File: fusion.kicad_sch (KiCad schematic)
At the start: 49 parts, among them J1 Conn_01x04_Female, J2 USB_C_Receptacle_USB2.0, J3 Conn_01x12_MountingPin, J4 Conn_01x12_MountingPin, K19 diode-choc, K20 diode-choc, K21 diode-choc, K22 diode-choc, K23 diode-choc, K24 diode-choc, K25 diode-choc, K26 diode-choc, K27 diode-choc, K28 diode-choc, K29 diode-choc, K30 diode-choc, K31 diode-choc, K32 diode-choc, K33 diode-choc, K34 diode-choc, K35 diode-choc, K36 diode-choc, K37 diode-choc, K38 diode-choc, SW1 SW_Push, U1 Holyiot_18010, U2 MT25QL128ABA1ESE

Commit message: final?
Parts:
- removed D42: SK6812MINI, LED_SMD:LED_SK6812MINI_PLCC4_3.5x3.5mm_P1.75mm, symbol LED:SK6812MINI
- removed U1: Holyiot_18010, keeb-libs:Holyiot-18010, symbol keeb-libs:Holyiot_18010
- added D2: LED_RBAG, fusion:FM-B2020RGBA, symbol Device:LED_RBAG
- added H15: sensor-magnet, fusion:sensor-magnet, symbol Mechanical:MountingHole
- added H16, H17, H18, H19: mount-magnet, fusion:mount-magnet, symbol Mechanical:MountingHole
- added R12: 1.2k, Resistor_SMD:R_0603_1608Metric, symbol Device:R
- added R13: 1.5k, Resistor_SMD:R_0603_1608Metric, symbol Device:R
- added R14: 1k, Resistor_SMD:R_0603_1608Metric, symbol Device:R
- added U1: Holyiot_18010_no_underside, keeb-libs:Holyiot-18010-no-underside, symbol keeb-libs:Holyiot_18010_no_underside
- H10, H7, H8, H9: value hinge -> mount-magnet; footprint fusion:hinge -> fusion:mount-magnet
- J1: footprint keeb-libs:debug-port -> keeb-libs:debug-port-single-side
- R3: value 10k -> 100k
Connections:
- net BAT_MEAS: now also U1.11 ([L]_A7_P0.31)
- net C0: now also U1.39 ([L]_P1.02)
- net C1: now also U1.36 ([L]_P1.04)
- net C2: now also U1.35 ([L]_P1.06)
- net C3: now also U1.34 ([L]_P0.09)
- net C4: now also U1.33 ([L]_P0.10)
- net D+: now also U1.45 (D+)
- net D-: now also U1.46 (D-)
- net DISP_~{CS}: now also U1.6 ([L]_A1_P0.03)
- net FLASH_~{CS}: now also U1.8 ([L]_A4_P0.28)
- net GND: now also U1.1 (GND), U1.32 (GND), U1.44 (GND)
- net MISO_DQ1: now also U1.12 (A2_P0.04)
- net MOSI_DQ0: now also U1.13 (A3_P0.05)
- net MOTION: now also U1.7 ([L]_A0_P0.02)
- net R0: now also U1.5 ([L]_P1.15)
- net R1: now also U1.4 ([L]_P1.13)
- net R2: now also U1.3 ([L]_P1.10)
- net R3: now also U1.2 ([L]_P1.11)
- net R4: now also U1.41 ([L]_P1.03)
- net R5: now also U1.43 (P0.22)
- net R6: now also U1.52 (P0.12)
- net R7: now also U1.53 (P1.09)
- net RST: now also U1.48 (Reset/P0.18)
- net SCLK: now also U1.54 (P0.07)
- net SHTDWN: now also U1.9 ([L]_A5_P0.29)
- net SWC: now also J1.3 (Pin_3), U1.38 (SWC); no longer J1.4 (Pin_4)
- net SWD: now also J1.4 (Pin_4), U1.37 (SWD); no longer J1.3 (Pin_3)
- net TRACKPAD_~{CS}: now also U1.10 ([L]_A6_P0.30)
- net VBUS: now also U1.47 (VBUS)
- net VDD: now also D2.3 (A), U1.55 (VDD)
- new net: D2.4 (GK), R13.2
- new net: D2.1 (RK), R12.2
- new net: D2.2 (BK), R14.2
- new net MAGNET: U1.40 ([L]_P1.01)
- new net ~{BLUE}: R14.1, U1.49 (P0.19)
- new net ~{GREEN}: R13.1, U1.50 (P0.21)
- new net ~{RED}: R12.1, U1.51 (P0.23)
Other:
- removed sheet trackpad_conn
- added sheet trackpad-8520 (trackpad-8520.kicad_sch)
- sheet power ports: added MAGNET; removed GND
- moved on the sheet: H11, H12, H13, H14, H3, H4

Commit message: backup
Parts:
- removed D2: LED_RBAG, fusion:FM-B2020RGBA, symbol Device:LED_RBAG
- removed H10, H16, H19: mount-magnet, fusion:mount-magnet, symbol Mechanical:MountingHole
- added D2: LED_RABG, LED_SMD:LED_ASMB-KTF0-0A306, symbol Device:LED_RABG
- added H20: bat-cover, fusion:bat-cover, symbol Mechanical:MountingHole
- added H21, H22, H23, H24: hinge-mousebite, fusion:hinge-mousebite, symbol Mechanical:MountingHole
- added JP1, JP2, JP3: SolderJumper_2_Open, Jumper:SolderJumper-2_P1.3mm_Open_RoundedPad1.0x1.5mm, symbol Jumper:SolderJumper_2_Open
- added U8: SRV05-4, Package_TO_SOT_SMD:SOT-23-6, symbol Power_Protection:SRV05-4
- H7: value mount-magnet -> hinge; footprint fusion:mount-magnet -> fusion:hinge
- K19, K24, K29: footprint pg1232:pg1232-DSSL -> pg1232:pg1232-DSSN
- K20, K25, K30: footprint pg1232:pg1232-DSSR -> pg1232:pg1232-DSSL
- K22, K27, K32: footprint pg1232:pg1232-DSSL -> pg1232:pg1232-DSSR
- K23, K28, K33: footprint pg1232:pg1232-DSSN -> pg1232:pg1232-DSSL
- K34, K35: footprint pg1232:pg1232-DSS -> pg1232:pg1232-DSSN
- K37, K38: footprint pg1232:pg1232-DSSN -> pg1232:pg1232-DSS
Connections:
- net C0: now also J4.4 (Pin_4), U1.2 ([L]_P1.11); no longer J4.12 (Pin_12), U1.39 ([L]_P1.02)
- net C1: now also J4.5 (Pin_5), U1.3 ([L]_P1.10); no longer J4.11 (Pin_11), U1.36 ([L]_P1.04)
- net C2: now also J4.6 (Pin_6), U1.4 ([L]_P1.13); no longer J4.10 (Pin_10), U1.35 ([L]_P1.06)
- net C3: now also J4.7 (Pin_7), U1.5 ([L]_P1.15); no longer J4.9 (Pin_9), U1.34 ([L]_P0.09)
- net D+: now also U8.3 (IO2), U8.4 (IO3)
- net D-: now also U8.1 (IO1), U8.6 (IO4)
- net FLASH_~{CS}: now also U1.53 (P1.09); no longer U1.8 ([L]_A4_P0.28)
- net GND: now also U8.2 (VN)
- net MISO_DQ1: now also JP2.2 (B)
- net MOSI_DQ0: now also JP3.2 (B)
- net R0: now also J4.9 (Pin_9), U1.34 ([L]_P0.09); no longer J4.7 (Pin_7), U1.5 ([L]_P1.15)
- net R1: now also J4.10 (Pin_10), U1.35 ([L]_P1.06); no longer J4.6 (Pin_6), U1.4 ([L]_P1.13)
- net R2: now also J4.11 (Pin_11), U1.36 ([L]_P1.04); no longer J4.5 (Pin_5), U1.3 ([L]_P1.10)
- net R3: now also J4.12 (Pin_12), U1.39 ([L]_P1.02); no longer J4.4 (Pin_4), U1.2 ([L]_P1.11)
- net R7: now also U1.8 ([L]_A4_P0.28); no longer U1.53 (P1.09)
- net SCLK: now also JP1.2 (B)
- net VBUS: now also U8.5 (VP)
- net VDD: now also D2.2 (A)
- net left/BAT: now also J3.12 (Pin_12); no longer J3.1 (Pin_1)
- net left/C0: now also J3.9 (Pin_9); no longer J3.12 (Pin_12)
- net left/C1: now also J3.8 (Pin_8); no longer J3.11 (Pin_11)
- net left/C2: now also J3.7 (Pin_7); no longer J3.10 (Pin_10)
- net left/C3: now also J3.6 (Pin_6); no longer J3.9 (Pin_9)
- net left/C4: now also J3.5 (Pin_5); no longer J3.8 (Pin_8)
- net left/GND: now also J3.11 (Pin_11); no longer J3.2 (Pin_2)
- net left/R0: now also J3.4 (Pin_4); no longer J3.7 (Pin_7)
- net left/R1: now also J3.3 (Pin_3); no longer J3.6 (Pin_6)
- net left/R2: now also J3.2 (Pin_2); no longer J3.5 (Pin_5)
- net left/R3: now also J3.1 (Pin_1); no longer J3.4 (Pin_4)
- net at R13.2: now also D2.4 (GK)
- net at R12.2: now also D2.1 (RK)
- net at R14.2: now also D2.3 (BK)
- new net trackpad-8520/MISO_2V8: JP2.1 (A)
- new net trackpad-8520/MOSI_3V3: JP3.1 (A)
- new net trackpad-8520/SCK_3V3: JP1.1 (A)
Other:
- moved on the sheet: H11, H13, H3, H4, H5, H6, J2, J3, R7, R9

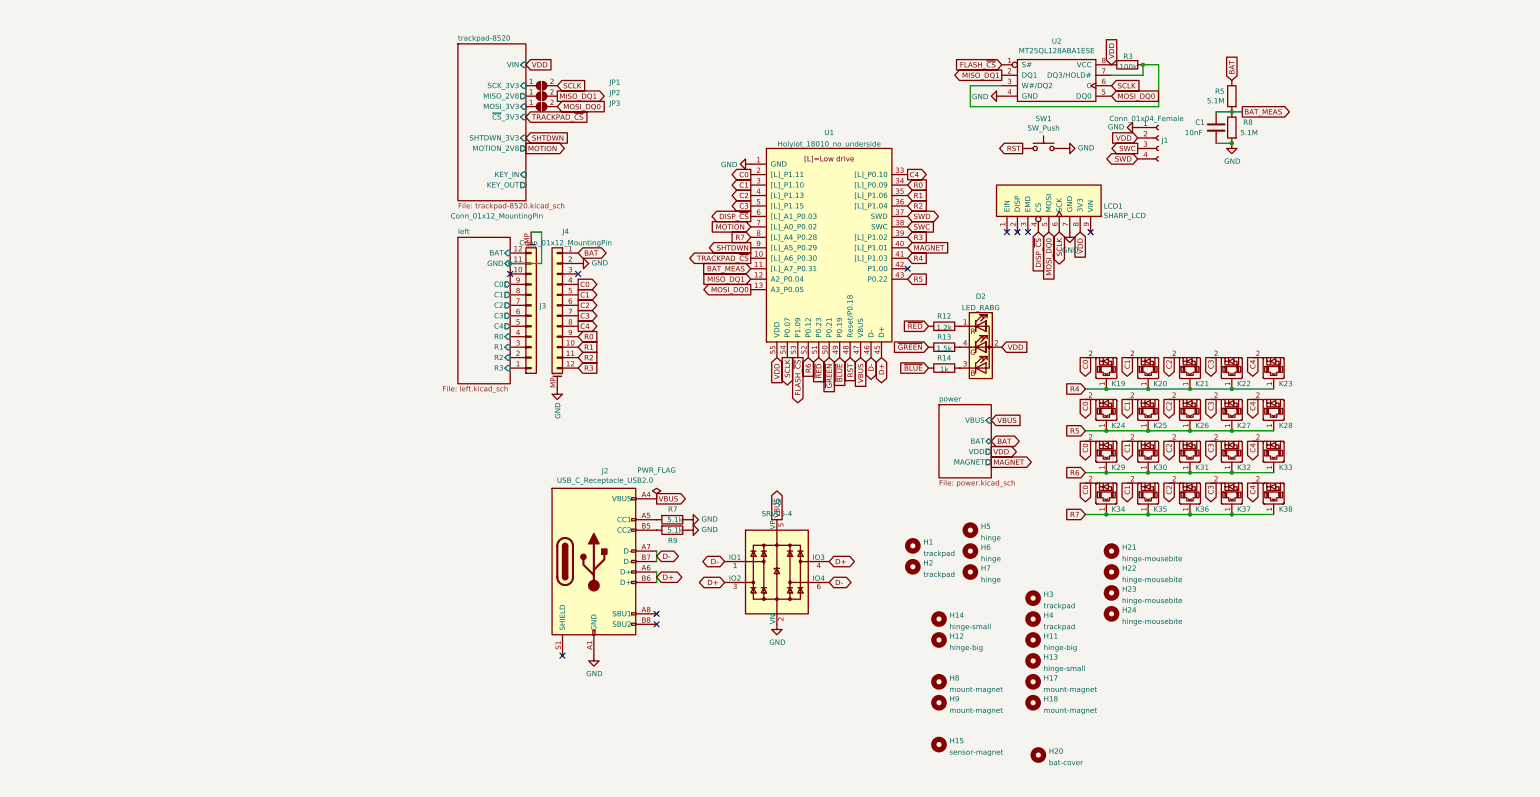
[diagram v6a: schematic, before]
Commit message: Hydrogen.PCB
- add Adafruit CAD files for Sharp display
- convert to all 3D printed mechanical parts
- update part dimensions to lowest estimate
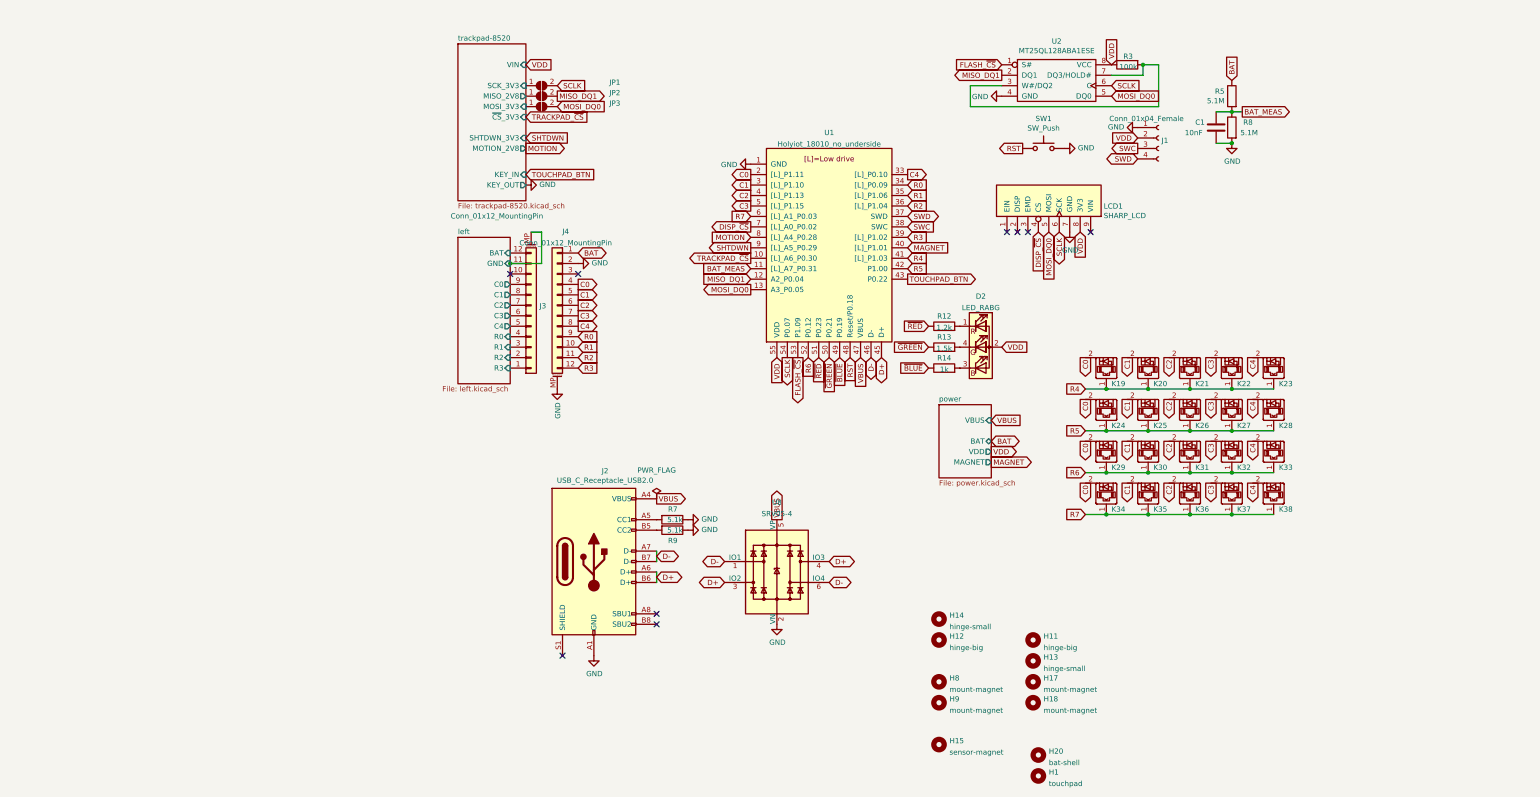
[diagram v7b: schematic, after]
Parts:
- removed H2, H3, H4: trackpad, fusion:trackpad, symbol Mechanical:MountingHole
- removed H21, H22, H23, H24: hinge-mousebite, fusion:hinge-mousebite, symbol Mechanical:MountingHole
- removed H5, H6, H7: hinge, fusion:hinge, symbol Mechanical:MountingHole
- D2, H15, H17, H18, H8, H9, J1, J3, J4, LCD1, U1: now left out of the parts list
- H1: value trackpad -> touchpad; footprint fusion:trackpad -> fusion:touchpad-holder; now left out of the parts list
- H11, H12: footprint fusion:hinge-big -> fusion:hinge2; now left out of the parts list
- H13, H14: footprint fusion:hinge-small -> fusion:hinge1; now left out of the parts list
- H20: value bat-cover -> bat-shell; footprint fusion:bat-cover -> fusion:bat-shell; now left out of the parts list
- SW1: footprint Button_Switch_SMD:SW_SPST_B3U-1000P -> Button_Switch_SMD:SW_SPST_TL3342
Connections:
- net DISP_~{CS}: now also U1.7 ([L]_A0_P0.02); no longer U1.6 ([L]_A1_P0.03)
- net MOTION: now also U1.8 ([L]_A4_P0.28); no longer U1.7 ([L]_A0_P0.02)
- net R5: now also U1.42 (P1.00); no longer U1.43 (P0.22)
- net R7: now also U1.6 ([L]_A1_P0.03); no longer U1.8 ([L]_A4_P0.28)
- new net TOUCHPAD_BTN: U1.43 (P0.22)
- no-connect marks 10 -> 9

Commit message: update PCB
use cirque trackpad, increase angle to 22.5
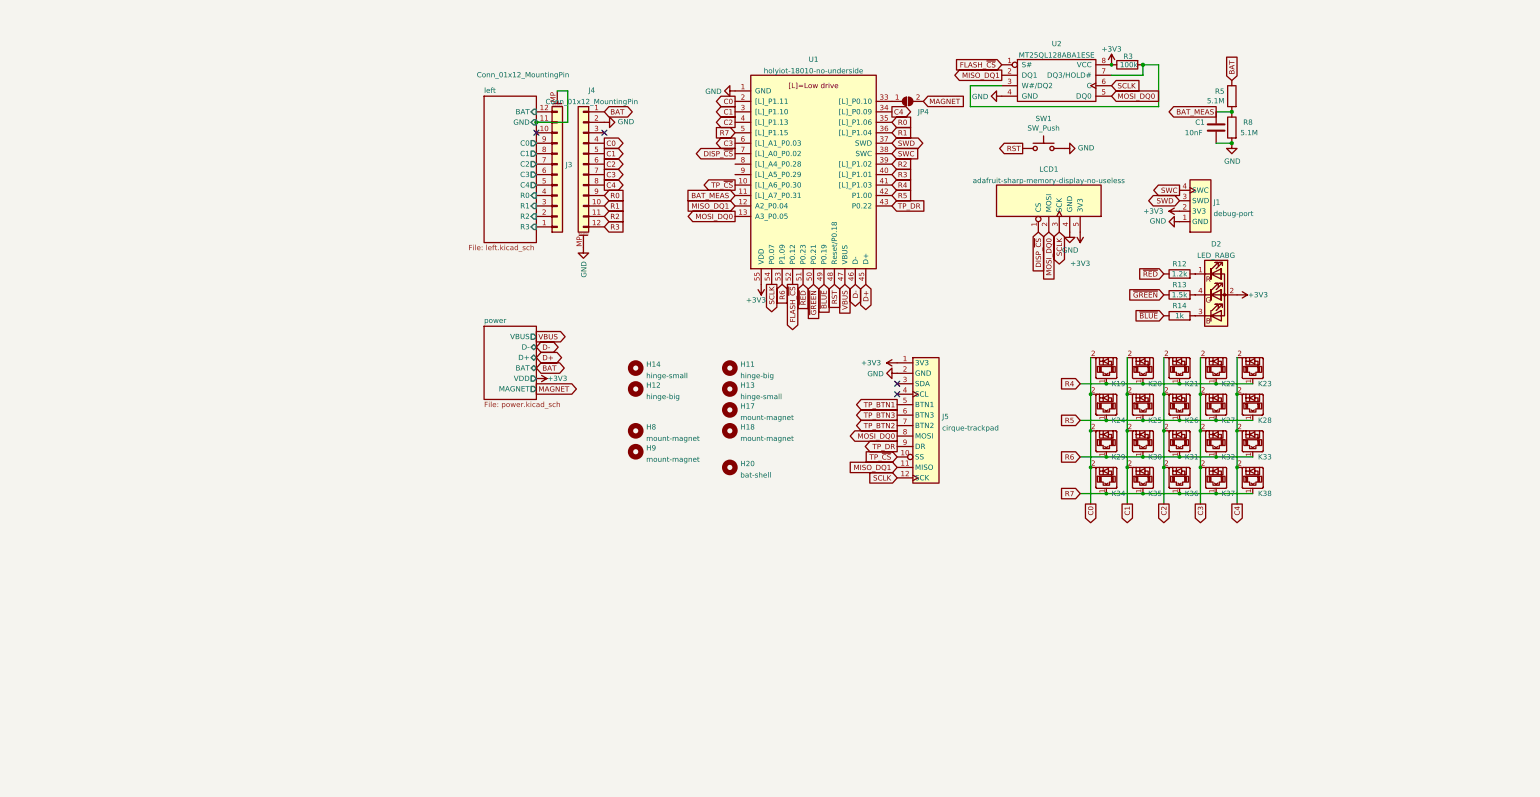
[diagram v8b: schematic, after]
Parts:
- removed H1: touchpad, fusion:touchpad-holder, symbol Mechanical:MountingHole
- removed H15: sensor-magnet, fusion:sensor-magnet, symbol Mechanical:MountingHole
- removed J1: Conn_01x04_Female, keeb-libs:debug-port-single-side, symbol Connector:Conn_01x04_Female
- removed J2: USB_C_Receptacle_USB2.0, Connector_USB:USB_C_Receptacle_HRO_TYPE-C-31-M-12, symbol Connector:USB_C_Receptacle_USB2.0
- removed JP1, JP2, JP3: SolderJumper_2_Open, Jumper:SolderJumper-2_P1.3mm_Open_RoundedPad1.0x1.5mm, symbol Jumper:SolderJumper_2_Open
- removed LCD1: SHARP_LCD, keeb-libs:Adafruit-Sharp-Memory-Display-1.3in-no-mounting, symbol keeb-libs:SHARP_LCD
- removed R7, R9: 5.1k, Resistor_SMD:R_0603_1608Metric, symbol Device:R
- removed U1: Holyiot_18010_no_underside, keeb-libs:Holyiot-18010-no-underside, symbol keeb-libs:Holyiot_18010_no_underside
- removed U2: MT25QL128ABA1ESE, Package_SO:SOP-8_5.28x5.23mm_P1.27mm, symbol steno:MT25QL128ABA1ESE
- removed U8: SRV05-4, Package_TO_SOT_SMD:SOT-23-6, symbol Power_Protection:SRV05-4
- added J1: debug-port, misc:debug-port-single-side, symbol misc:debug-port
- added J5: cirque-trackpad, Connector_FFC-FPC:Hirose_FH12-12S-0.5SH_1x12-1MP_P0.50mm_Horizontal, symbol misc:cirque-trackpad
- added JP4: SolderJumper_2_Open, Jumper:SolderJumper-2_P1.3mm_Open_RoundedPad1.0x1.5mm, symbol Jumper:SolderJumper_2_Open
- added LCD1: adafruit-sharp-memory-display-no-useless, display:adafruit-sharp-memory-display-1.3in-no-mounting-no-useless, symbol display:adafruit-sharp-memory-display-no-useless
- added U1: holyiot-18010-no-underside, mcu:holyiot-18010-no-underside, symbol mcu:holyiot-18010-no-underside
- added U2: MT25QL128ABA1ESE, Package_SO:SOIC-8_5.23x5.23mm_P1.27mm, symbol ic:MT25QL128ABA1ESE
- H20: footprint fusion:bat-shell -> fusion:bat-shell-small
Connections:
- net BAT_MEAS: now also U1.11 ([L]_A7_P0.31)
- net C0: now also U1.2 ([L]_P1.11)
- net C1: now also U1.3 ([L]_P1.10)
- net C2: now also U1.4 ([L]_P1.13)
- net C3: now also U1.6 ([L]_A1_P0.03)
- net C4: now also U1.34 ([L]_P0.09)
- net D+: now also U1.45 (D+)
- net D-: now also U1.46 (D-)
- net DISP_~{CS}: now also LCD1.1 (CS), U1.7 ([L]_A0_P0.02)
- net FLASH_~{CS}: now also U1.52 (P0.12), U2.1 (S#)
- net GND: now also J1.1 (GND), J5.2 (GND), LCD1.4 (GND), U1.1 (GND), U1.32 (GND), U1.44 (GND), U2.4 (GND)
- net MAGNET: now also JP4.2 (B)
- net MISO_DQ1: now also J5.11 (MISO), U1.12 (A2_P0.04), U2.2 (DQ1)
- net MOSI_DQ0: now also J5.8 (MOSI), LCD1.2 (MOSI), U1.13 (A3_P0.05), U2.5 (DQ0)
- net R0: now also U1.35 ([L]_P1.06)
- net R1: now also U1.36 ([L]_P1.04)
- net R2: now also U1.39 ([L]_P1.02)
- net R3: now also U1.40 ([L]_P1.01)
- net R4: now also U1.41 ([L]_P1.03)
- net R5: now also U1.42 (P1.00)
- net R6: now also U1.53 (P1.09)
- net R7: now also U1.5 ([L]_P1.15)
- net RST: now also U1.48 (Reset/P0.18)
- net SCLK: now also J5.12 (SCK), LCD1.3 (SCK), U1.54 (P0.07), U2.6 (C)
- net SWC: now also J1.4 (SWC), U1.38 (SWC)
- net SWD: now also J1.3 (SWD), U1.37 (SWD)
- net VBUS: now also U1.47 (VBUS)
- net ~{BLUE}: now also U1.49 (P0.19)
- net ~{GREEN}: now also U1.50 (P0.21)
- net ~{RED}: now also U1.51 (P0.23)
- net at R3.2: now also U2.3 (W#/DQ2), U2.7 (DQ3/HOLD#)
- net VDD renamed +3V3
- net +3V3: now also J1.2 (3V3), J5.1 (3V3), LCD1.5 (3V3), U1.55 (VDD), U2.8 (VCC)
- new net: JP4.1 (A), U1.33 ([L]_P0.10)
- new net TP_BTN1: J5.5 (BTN1)
- new net TP_BTN2: J5.7 (BTN2)
- new net TP_BTN3: J5.6 (BTN3)
- new net TP_DR: J5.9 (DR), U1.43 (P0.22)
- new net TP_~{CS}: J5.10 (SS), U1.10 ([L]_A6_P0.30)
- no-connect marks 9 -> 4
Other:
- removed sheet trackpad-8520
- sheet power ports: added D+, D-; removed none
- moved on the sheet: D2, H11, H12, H13, H14, H17, H18, H20, H8, H9, J3, J4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
